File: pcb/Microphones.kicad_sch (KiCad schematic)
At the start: 40 parts, among them J16 Conn_02x01, U1 AD8426ACPZ-R7, U2 AD8426ACPZ-R7, U3 LT1790ACS6-1.25

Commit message: Polishin pt1
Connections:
- net at MK2.3 (OUTPUT-): now also R6.2; no longer R6.1
- net mic2_out2: now reaches C12.2, C29.2, U1.9 (+IN2)
- net mic2_out2: now also R6.1; no longer R6.2
- net mic3_out1: now reaches C5.2, C6.1, R8.2, U2.1 (-IN1)
- net mic4_out1: now reaches C16.2, R10.2, U2.12 (-IN2)
- net mic4_out1: now also C17.2; no longer C17.1
- net mic3_out2: now reaches C6.2, C9.2, R9.2, U2.4 (+IN1)
- net mic4_out2: now reaches C18.2, R11.2, U2.9 (+IN2)
- net mic4_out2: now also C17.1; no longer C17.2
- net mic2_out1: now reaches C12.1, C28.2, R3.2, U1.12 (-IN2)
- net mic1_out2: now reaches C13.2, C31.2, R5.2, U1.4 (+IN1)
- net mic1_out1: now reaches C13.1, C30.2, R4.2, U1.1 (-IN1)
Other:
- note added: "MEMS MICROPHONES"
- note added: "MICROPHONE AMPLIFIERS"
- note added: "VOLTAGE REGULATOR 3.3V->1.25V"
- company: (none) -> Infineon Technologies
- title: (none) -> SensEdu 0.7
- moved on the sheet: C1, C10, C11, C12, C13, C14, C16, C17, C18, C2, C20, C28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

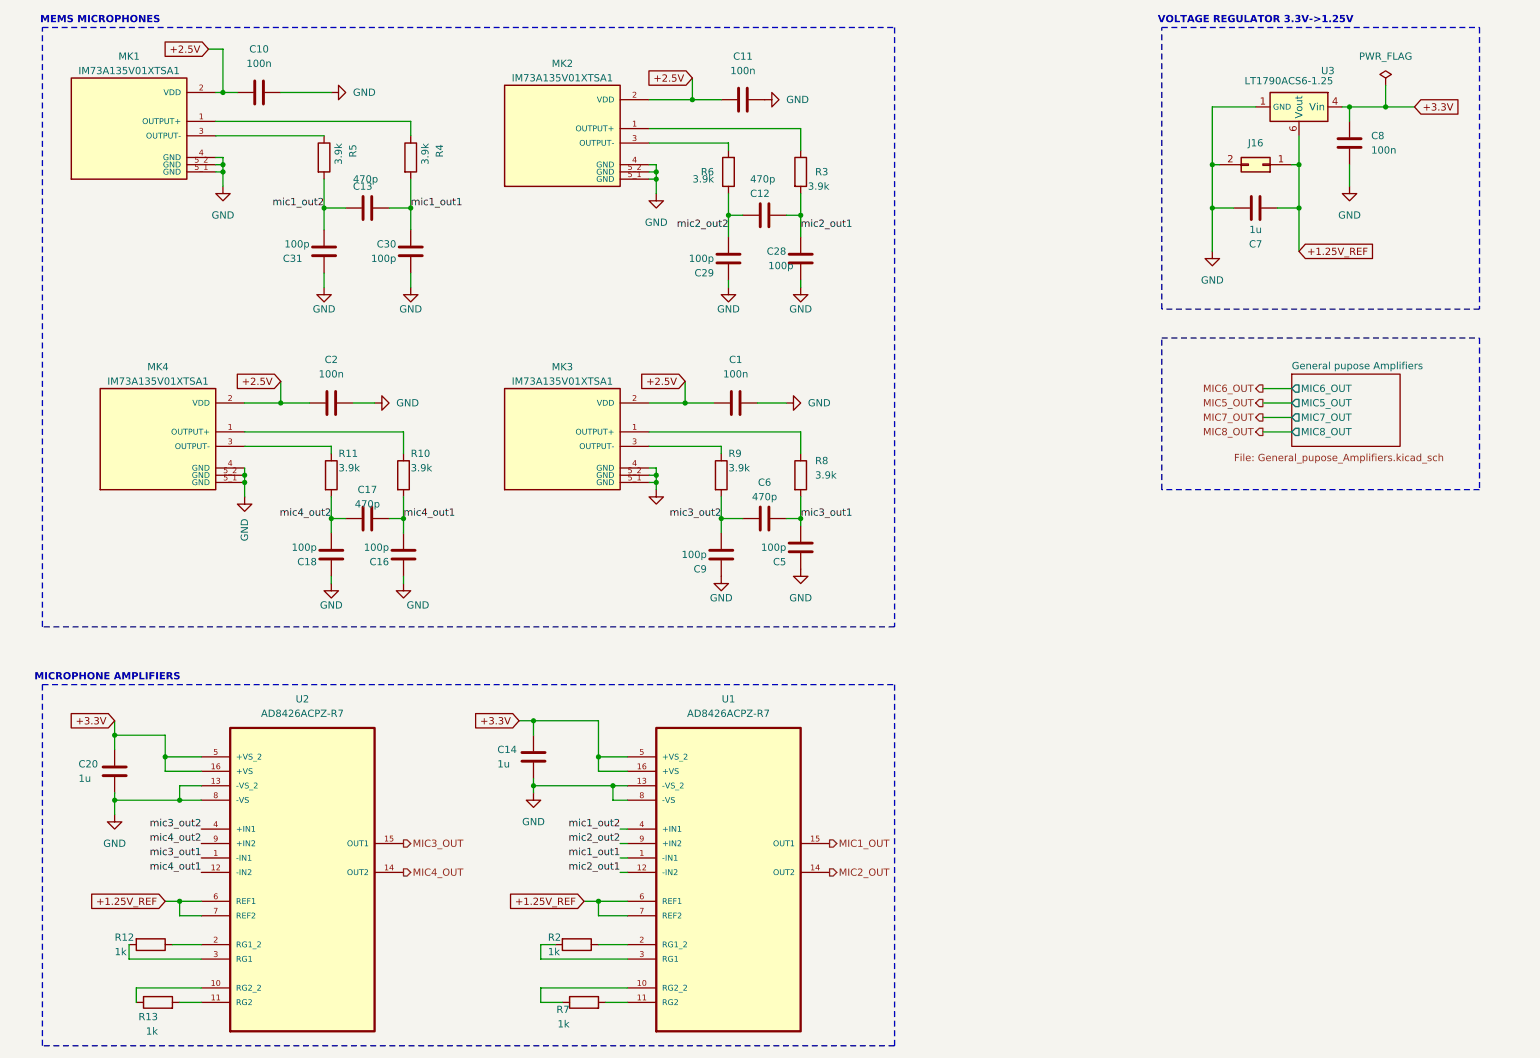
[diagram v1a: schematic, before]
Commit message: feat: Polished Sensedu schematics
Renamed Sheets
Added Nets
Repaired connections
Renamed Datasheets
Generated new schematic PDF
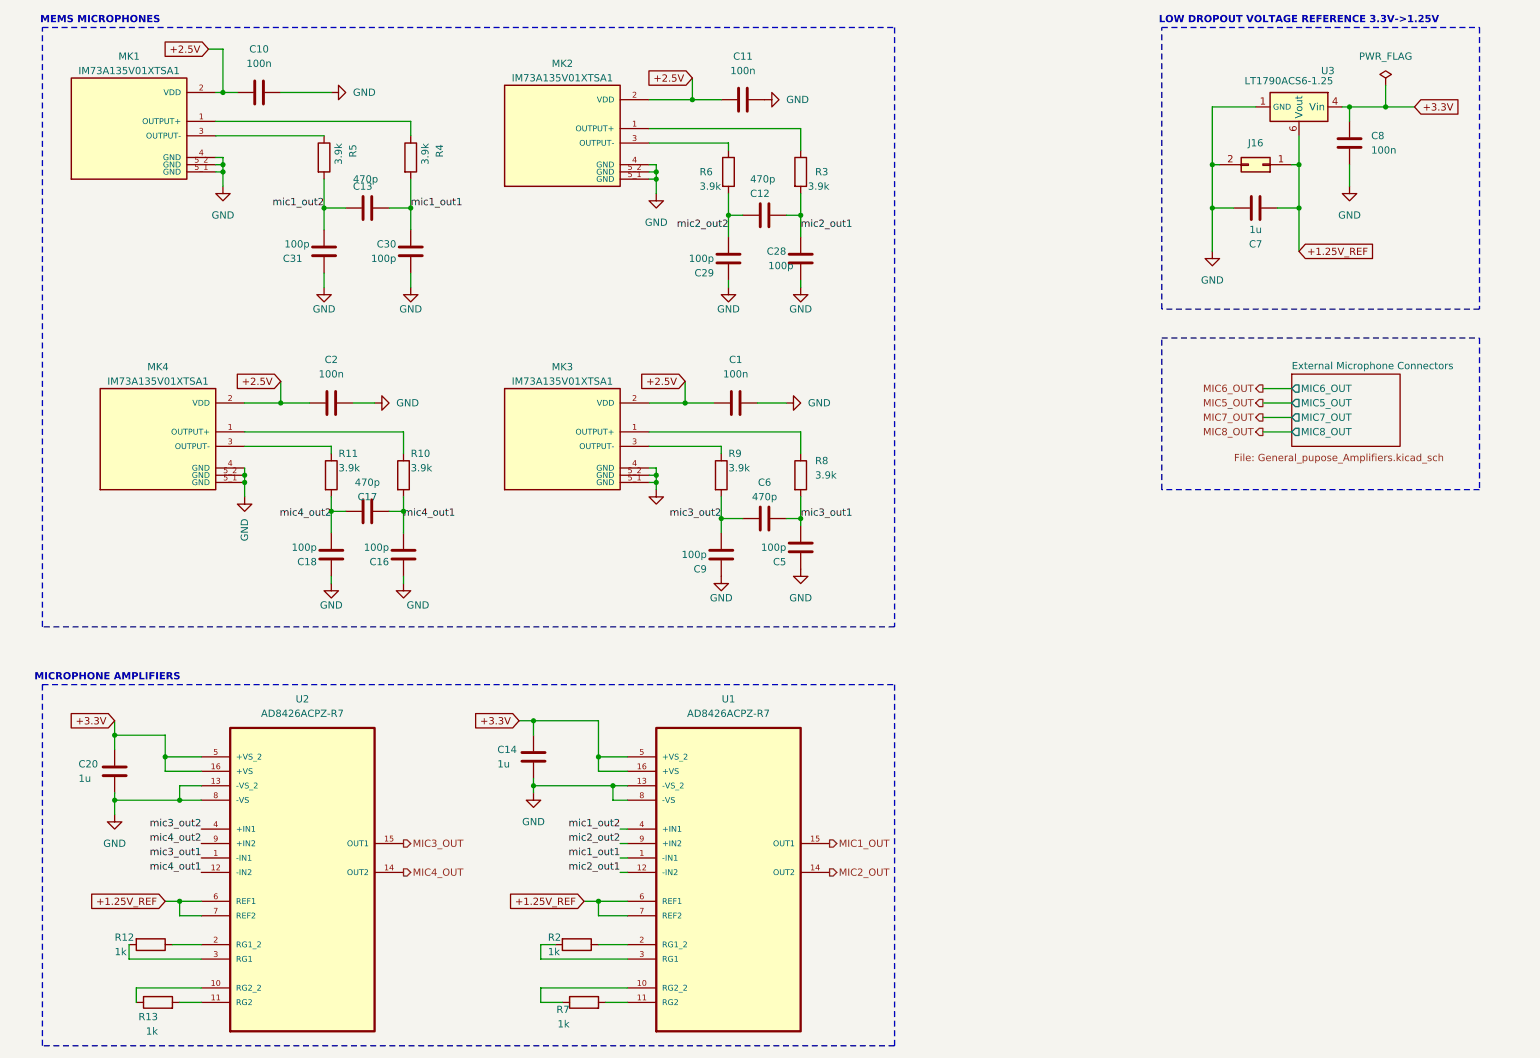
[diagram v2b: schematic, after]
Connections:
- net mic2_out2: now also R6.2; no longer R6.1
- net mic4_out1: now also C17.1; no longer C17.2
- net mic4_out2: now also C17.2; no longer C17.1
- net at MK2.3 (OUTPUT-): now also R6.1; no longer R6.2
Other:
- sheet General pupose Amplifiers renamed External Microphone Connectors
- note added: "LOW DROPOUT VOLTAGE REFERENCE 3.3V->1.25V"
- note removed: "VOLTAGE REGULATOR 3.3V->1.25V"
- moved on the sheet: C17, R6
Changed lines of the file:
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@@
 		)
 	)
-	(text "VOLTAGE REGULATOR 3.3V->1.25V"
+	(text "LOW DROPOUT VOLTAGE REFERENCE 3.3V->1.25V"
 		(exclude_from_sim yes)
-		(at 236.22 13.97 0)
+		(at 243.84 13.97 0)
 		(effects
 			(font
@@
 	)
 	(junction
-		(at 87.63 46.99)
+		(at 143.51 48.26)
 		(diameter 0)
 		(color 0 0 0 0)
 	)
 	(junction
-		(at 142.24 101.6)
+		(at 87.63 46.99)
 		(diameter 0)
 		(color 0 0 0 0)
 	)
 	(junction
-		(at 120.65 168.91)
+		(at 142.24 101.6)
 		(diameter 0)
 		(color 0 0 0 0)
 	)
 	(junction
-		(at 120.65 143.51)
+		(at 120.65 168.91)
 		(diameter 0)
 		(color 0 0 0 0)
 	)
 	(junction
-		(at 86.36 101.6)
+		(at 120.65 143.51)
 		(diameter 0)
 		(color 0 0 0 0)
@@
 	)
 	(junction
-		(at 109.22 137.16)
+		(at 73.66 100.33)
 		(diameter 0)
 		(color 0 0 0 0)
 	)
 	(junction
-		(at 143.51 48.26)
+		(at 109.22 137.16)
 		(diameter 0)
 		(color 0 0 0 0)
@@
 	)
 	(junction
-		(at 73.66 101.6)
+		(at 123.19 148.59)
 		(diameter 0)
 		(color 0 0 0 0)
 	)
 	(junction
-		(at 123.19 148.59)
+		(at 109.22 148.59)
 		(diameter 0)
 		(color 0 0 0 0)
 	)
 	(junction
-		(at 109.22 148.59)
+		(at 86.36 100.33)
 		(diameter 0)
 		(color 0 0 0 0)
@@
 	(wire
 		(pts
+			(xy 143.51 44.45) (xy 143.51 48.26)
+		)
+		(stroke
+			(width 0)
+			(type default)
+		)
+	)
+	(wire
+		(pts
 			(xy 156.21 90.17) (xy 156.21 86.36)
 		)
@@
 	(wire
 		(pts
-			(xy 86.36 101.6) (xy 86.36 104.14)
+			(xy 86.36 97.79) (xy 86.36 100.33)
 		)
 		(stroke
@@
 	(wire
 		(pts
-			(xy 73.66 101.6) (xy 76.2 101.6)
-		)
-		(stroke
-			(width 0)
-			(type default)
-		)
-	)
-	(wire
-		(pts
 			(xy 44.45 168.91) (xy 46.99 168.91)
 		)
@@
 	(wire
 		(pts
-			(xy 143.51 35.56) (xy 143.51 36.83)
-		)
-		(stroke
-			(width 0)
-			(type default)
-		)
-	)
-	(wire
-		(pts
 			(xy 123.19 151.13) (xy 123.19 148.59)
 		)
@@
 	(wire
 		(pts
-			(xy 73.66 97.79) (xy 73.66 101.6)
-		)
-		(stroke
-			(width 0)
-			(type default)
-		)
-	)
-	(wire
-		(pts
 			(xy 58.42 95.25) (xy 58.42 93.98)
 		)
@@
 	(wire
 		(pts
-			(xy 83.82 101.6) (xy 86.36 101.6)
-		)
-		(stroke
-			(width 0)
-			(type default)
-		)
-	)
-	(wire
-		(pts
 			(xy 73.66 113.03) (xy 73.66 111.76)
 		)
@@
 	(wire
 		(pts
+			(xy 86.36 100.33) (xy 86.36 104.14)
+		)
+		(stroke
+			(width 0)
+			(type default)
+		)
+	)
+	(wire
+		(pts
 			(xy 109.22 137.16) (xy 109.22 139.7)
 		)
@@
 	(wire
 		(pts
-			(xy 73.66 101.6) (xy 73.66 104.14)
+			(xy 73.66 97.79) (xy 73.66 100.33)
 		)
 		(stroke
@@
 	(wire
 		(pts
-			(xy 53.34 40.64) (xy 54.61 40.64)
+			(xy 73.66 100.33) (xy 73.66 104.14)
 		)
 		(stroke
@@
 	(wire
 		(pts
-			(xy 39.37 184.15) (xy 50.8 184.15)
+			(xy 53.34 40.64) (xy 54.61 40.64)
 		)
 		(stroke
@@
 	(wire
 		(pts
-			(xy 54.61 38.1) (xy 54.61 39.37)
+			(xy 39.37 184.15) (xy 50.8 184.15)
 		)
 		(stroke
@@
 	(wire
 		(pts
-			(xy 110.49 186.69) (xy 114.3 186.69)
+			(xy 54.61 38.1) (xy 54.61 39.37)
 		)
 		(stroke
@@
 	(wire
 		(pts
-			(xy 86.36 97.79) (xy 86.36 101.6)
+			(xy 110.49 186.69) (xy 114.3 186.69)
 		)
 		(stroke
@@
 	(wire
 		(pts
+			(xy 73.66 100.33) (xy 76.2 100.33)
+		)
+		(stroke
+			(width 0)
+			(type default)
+		)
+	)
+	(wire
+		(pts
 			(xy 39.37 186.69) (xy 39.37 184.15)
 		)
@@
 	(wire
 		(pts
+			(xy 83.82 100.33) (xy 86.36 100.33)
+		)
+		(stroke
+			(width 0)
+			(type default)
+		)
+	)
+	(wire
+		(pts
 			(xy 52.07 19.05) (xy 54.61 19.05)
 		)
@@
 	(wire
 		(pts
-			(xy 143.51 44.45) (xy 143.51 48.26)
+			(xy 143.51 35.56) (xy 143.51 36.83)
 		)
 		(stroke
@@
 	(symbol
 		(lib_id "Device:R")
-		(at 143.51 40.64 180)
+		(at 143.51 40.64 0)
 		(unit 1)
 		(exclude_from_sim no)
@@
 		(dnp no)
 		(property "Reference" "R6"
-			(at 140.97 40.64 0)
+			(at 138.43 40.64 0)
 			(effects
 				(font
@@
 		)
 		(property "Value" "3.9k"
-			(at 140.97 41.91 0)
+			(at 138.43 43.18 0)
 			(effects
 				(font
@@
 		)
 		(property "Footprint" "Resistor_SMD:R_0805_2012Metric"
-			(at 145.288 40.64 90)
+			(at 141.732 40.64 90)
 			(effects
 				(font
@@
 	(symbol
 		(lib_id "Device:C")
-		(at 80.01 101.6 90)
+		(at 80.01 100.33 270)
 		(unit 1)
 		(exclude_from_sim no)
@@
 		(dnp no)
 		(property "Reference" "C17"
-			(at 80.01 96.52 90)
+			(at 80.01 97.79 90)
 			(effects
 				(font
@@
 		)
 		(property "Value" "470p"
-			(at 80.01 99.06 90)
+			(at 80.01 95.25 90)
 			(effects
 				(font
@@
 		)
 		(property "Footprint" "Capacitor_SMD:C_0805_2012Metric"
-			(at 83.82 100.6348 0)
+			(at 76.2 101.2952 0)
 			(effects
 				(font
@@
 		)
 		(property "Datasheet" "~"
-			(at 80.01 101.6 0)
+			(at 80.01 100.33 0)
 			(effects
 				(font
@@
 		)
 		(property "Description" ""
-			(at 80.01 101.6 0)
+			(at 80.01 100.33 0)
 			(effects
 				(font
@@
 			(color 0 0 0 0.0000)
 		)
-		(property "Sheetname" "General pupose Amplifiers"
+		(property "Sheetname" "External Microphone Connectors"
 			(at 242.57 75.4884 0)
 			(effects

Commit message: refactor: Edit speaker/mic symbols and polish
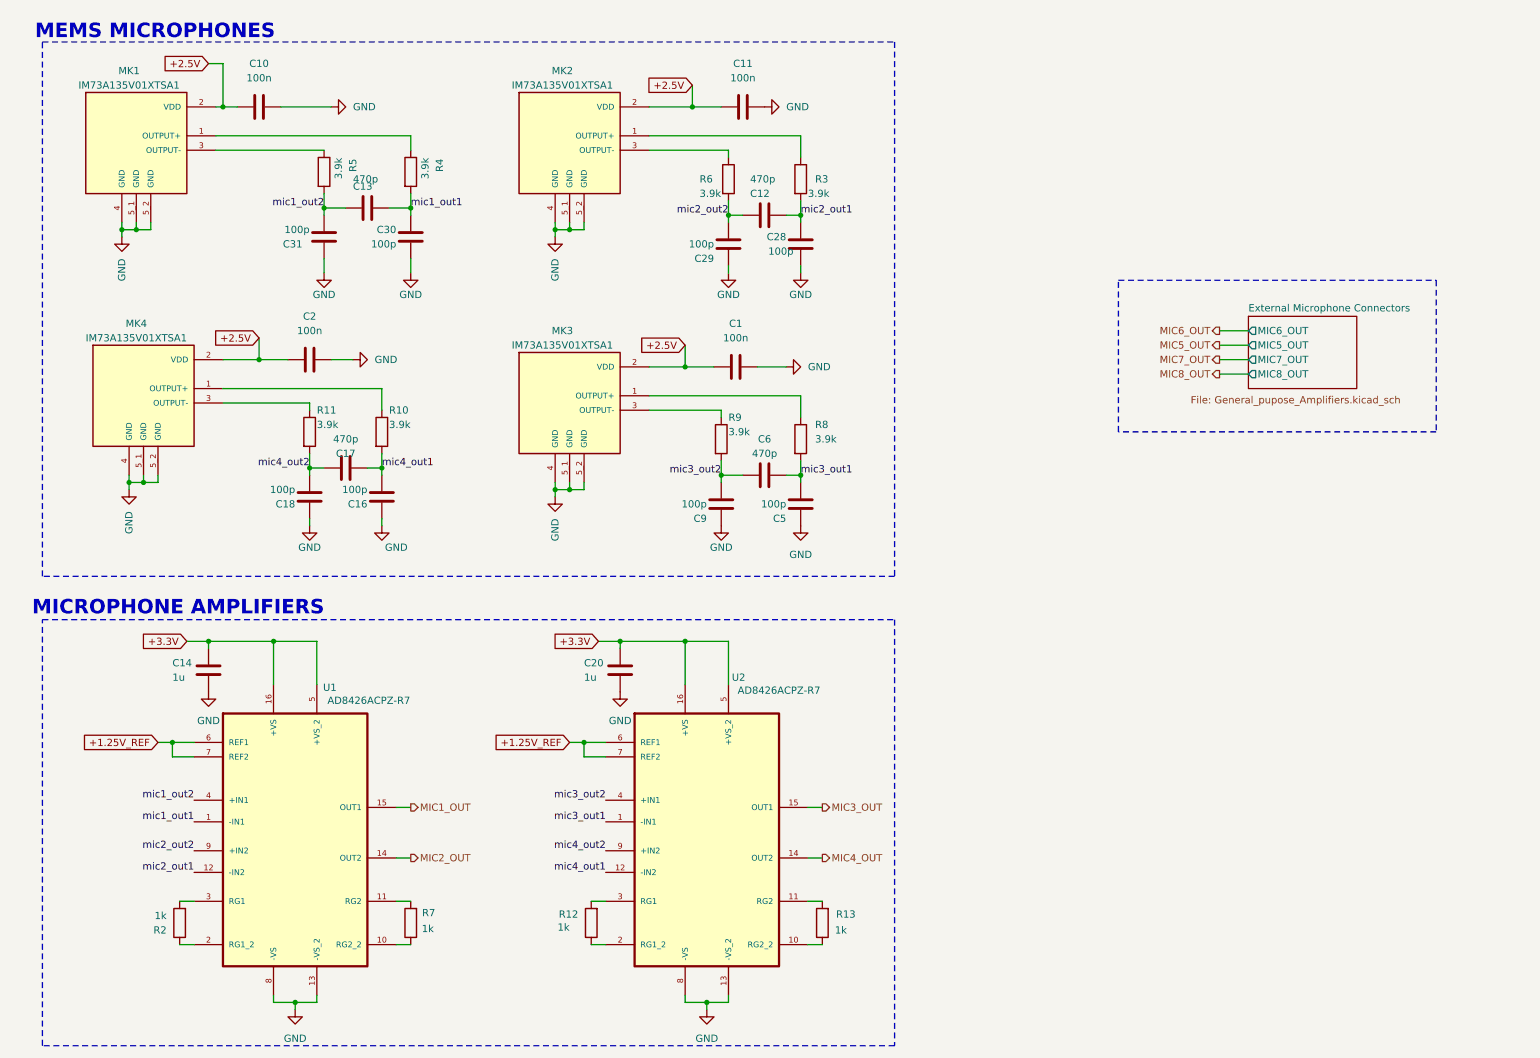
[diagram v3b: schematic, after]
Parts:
- removed C7: 1u, Capacitor_SMD:C_0805_2012Metric, symbol Device:C
- removed C8: 100n, Capacitor_SMD:C_0805_2012Metric, symbol Device:C
- removed J16: Conn_02x01, Connector_PinSocket_2.54mm:PinSocket_1x02_P2.54mm_Vertical, symbol Connector_Generic:Conn_02x01
- removed U3: LT1790ACS6-1.25, Package_TO_SOT_SMD:TSOT-23-6, symbol SensEdu:LT1790-2.5_sensedu
- MK1, MK2, MK3, MK4: footprint SensEdu:MIC_IM73A135V01XTSA1 -> MIC_IM73A135V01XTSA1
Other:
- note removed: "LOW DROPOUT VOLTAGE REFERENCE 3.3V->1.25V"
- moved on the sheet: C1, C10, C11, C14, C16, C17, C18, C2, C20, C28, C29, C30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
